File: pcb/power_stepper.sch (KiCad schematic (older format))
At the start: 52 parts, among them J2 1757284, P3 CONN_02X02, U16 UCC12040, U17 ISO7762, U2 powerSTEP01

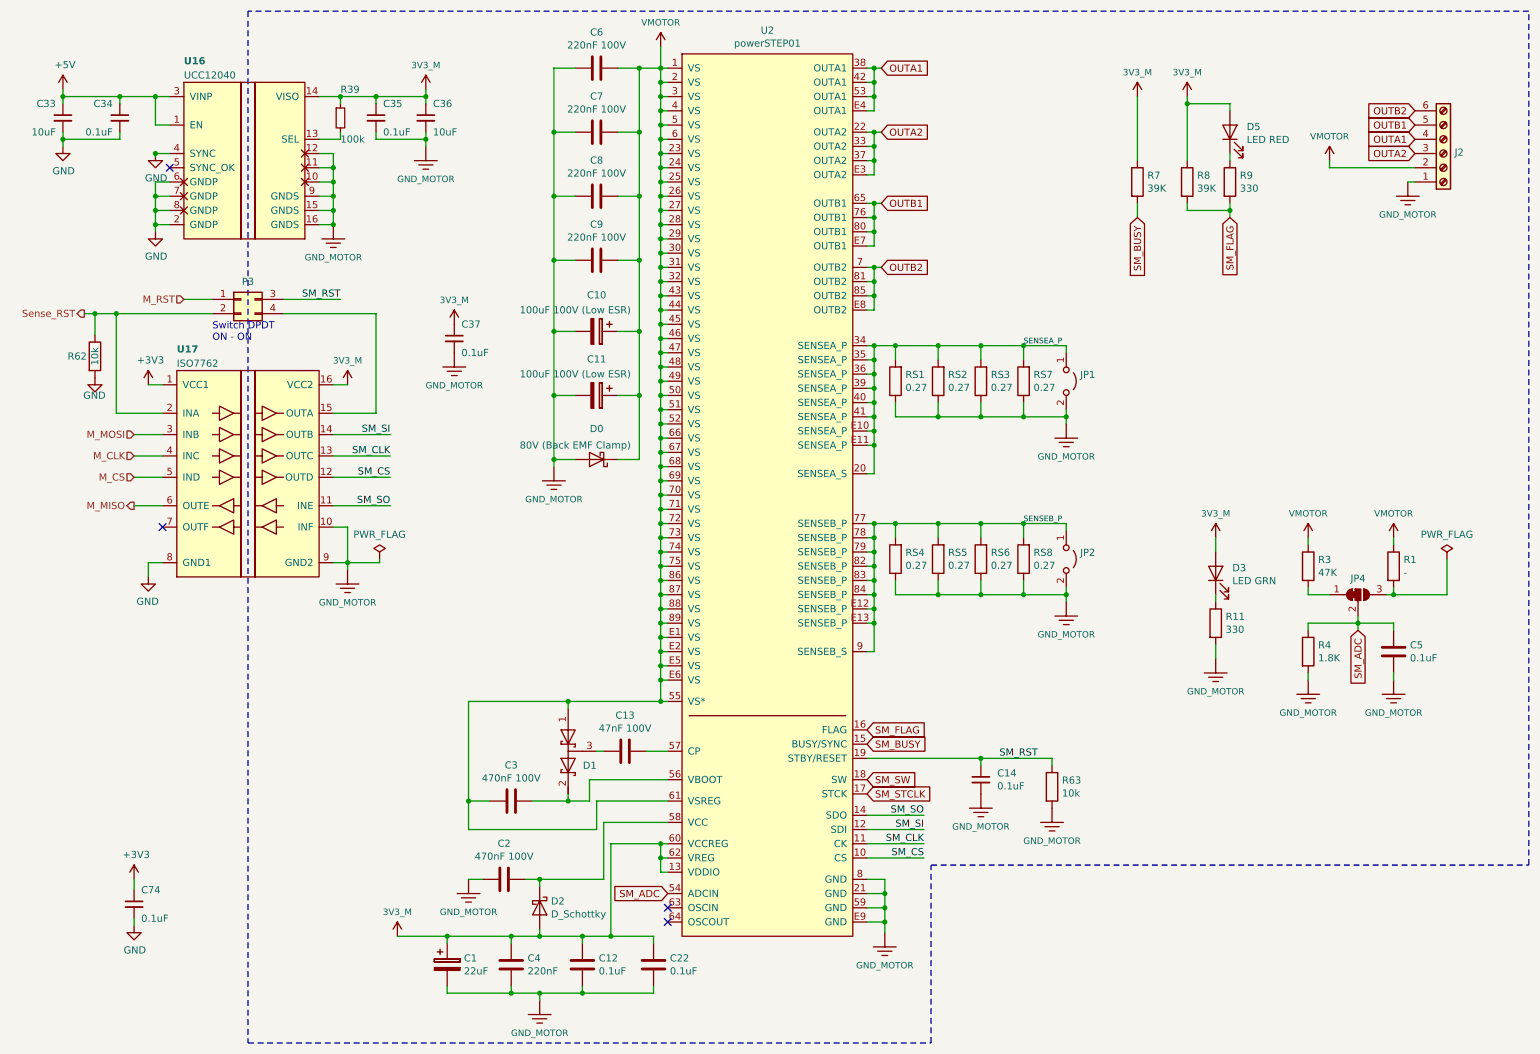
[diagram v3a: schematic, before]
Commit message: Chaged P3 to SW1 and a new circuit to emergency reset on IC powerstep01 Added 3d shape for 2 contancs molex clik-mate connector
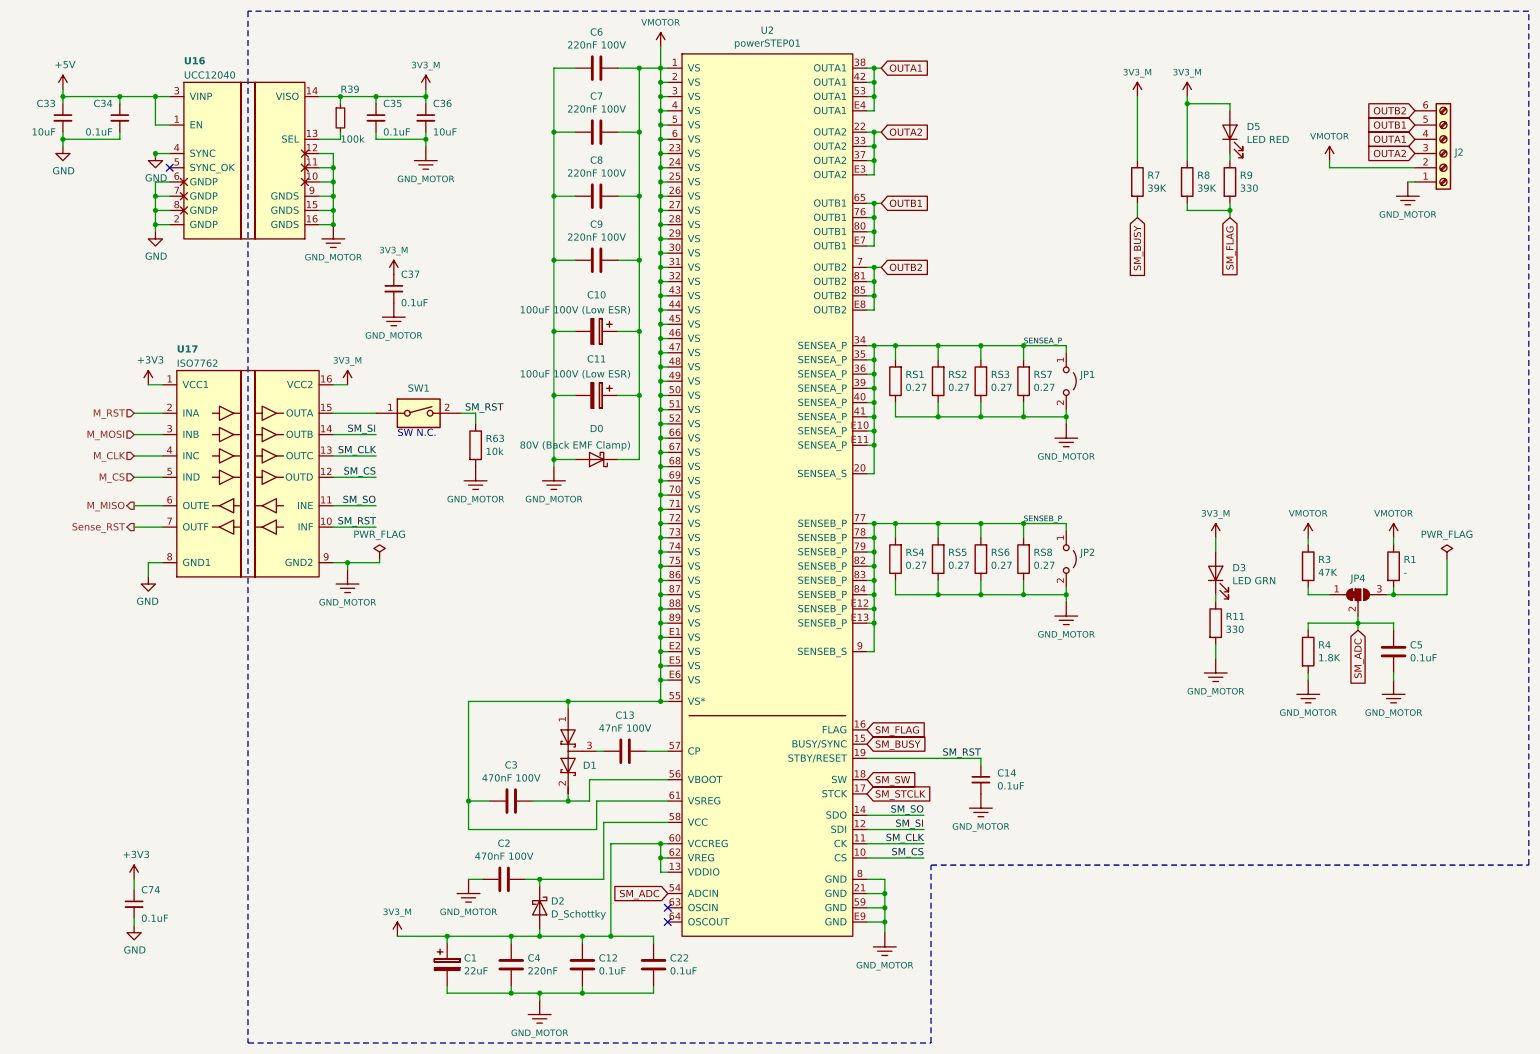
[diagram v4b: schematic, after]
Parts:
- removed P3: CONN_02X02, Connector_Molex:Molex_CLIK-Mate_502443-0470_1x04-1MP_P2.00mm_Vertical, symbol Connector_Generic:Conn_02x02_Top_Bottom
- removed R62: 10k, Resistor_SMD:R_0402_1005Metric, symbol Device:R
- added SW1: SW_DIP_x01, Connector_Molex:Molex_CLIK-Mate_502443-0270_1x02-1MP_P2.00mm_Vertical, symbol Switch:SW_DIP_x01
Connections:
- net GND_MOTOR: no longer U17.10 (INF)
- net M_RST: now also U17.2 (INA)
- net SM_RST: now also U17.10 (INF), SW1.2
- net Sense_RST: now also U17.7 (OUTF); no longer U17.2 (INA)
- net at U17.15 (OUTA): now also SW1.1
- no-connect marks 4 -> 3
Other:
- note added: "SW N.C."
- note removed: "Switch DPDT\nON - ON"
- moved on the sheet: C37, R63
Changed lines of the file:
@@
 Wire Wire Line
 	7250 5800 7250 5750
-Connection ~ 7250 5750
 Wire Wire Line
 	7850 3350 7850 3300
@@
 	2800 4375 2800 4425
 Wire Wire Line
-	2350 2525 2750 2525
-Text Label 2750 2525 2    50   ~ 0
+	3600 3325 3700 3325
+Text Label 3625 3325 0    50   ~ 0
 SM_RST
-Text Label 3100 3625 2    50   ~ 0
+Text Label 3000 3625 2    50   ~ 0
 SM_CLK
 Wire Wire Line
-	2700 3775 3100 3775
-Text Label 3100 3775 2    50   ~ 0
+	2700 3775 3000 3775
+Text Label 3000 3775 2    50   ~ 0
 SM_CS
 Wire Wire Line
-	2700 3975 3100 3975
-Text Label 3100 3975 2    50   ~ 0
+	2700 3975 3000 3975
+Text Label 3000 3975 2    50   ~ 0
 SM_SO
-Text Label 7650 5750 2    50   ~ 0
+Text Label 7250 5750 2    50   ~ 0
 SM_RST
 Wire Wire Line
@@
 L Device:C_Small C37
 U 1 1 5ED0B425
-P 3550 2800
-F 0 "C37" H 3600 2900 50  0000 L CNN
-F 1 "0.1uF" H 3600 2700 50  0000 L CNN
-F 2 "Capacitor_SMD:C_0402_1005Metric" H 3588 2650 50  0001 C CNN
-F 3 "~" H 3550 2800 50  0001 C CNN
-	1    3550 2800
+P 3125 2450
+F 0 "C37" H 3175 2550 50  0000 L CNN
+F 1 "0.1uF" H 3175 2350 50  0000 L CNN
+F 2 "Capacitor_SMD:C_0402_1005Metric" H 3163 2300 50  0001 C CNN
+F 3 "~" H 3125 2450 50  0001 C CNN
+	1    3125 2450
 	1    0    0    -1
 $EndComp
@@
 L ventilator-PowerSymbols:3V3_M #SUPPLY0111
 U 1 1 5ED0B439
-P 3550 2700
-F 0 "#SUPPLY0111" H 3600 2700 45  0001 L BNN
-F 1 "3V3_M" H 3550 2870 45  0000 C CNN
-F 2 "" H 3550 2700 50  0001 C CNN
-F 3 "" H 3550 2700 60  0001 C CNN
-	1    3550 2700
+P 3125 2350
+F 0 "#SUPPLY0111" H 3175 2350 45  0001 L BNN
+F 1 "3V3_M" H 3125 2520 45  0000 C CNN
+F 2 "" H 3125 2350 50  0001 C CNN
+F 3 "" H 3125 2350 60  0001 C CNN
+	1    3125 2350
 	1    0    0    -1
 $EndComp
 Wire Wire Line
 	2700 3125 2800 3125
-NoConn ~ 1500 4125
-Wire Wire Line
-	2700 4125 2800 4125
-Wire Wire Line
-	2800 4125 2800 4375
+Wire Wire Line
+	2700 4125 3000 4125
 Connection ~ 2800 4375
 Text HLabel 1300 3775 0    50   Input ~ 0
 M_CS
-Text HLabel 1650 2525 0    50   Input ~ 0
+Text HLabel 1300 3325 0    50   Input ~ 0
 M_RST
 Text HLabel 1300 3625 0    50   Input ~ 0
@@
 Wire Wire Line
 	1300 3775 1500 3775
-Wire Wire Line
-	1650 2525 1850 2525
 Wire Wire Line
 	1300 3625 1500 3625
@@
 L ventilator-PowerSymbols:GND_MOTOR #GND0114
 U 1 1 5EB73041
-P 3550 2900
-F 0 "#GND0114" H 3600 2850 45  0001 L BNN
-F 1 "GND_MOTOR" H 3550 2670 45  0000 C CNN
-F 2 "" H 3550 2900 50  0001 C CNN
-F 3 "" H 3550 2800 60  0001 C CNN
-	1    3550 2900
+P 3125 2550
+F 0 "#GND0114" H 3175 2500 45  0001 L BNN
+F 1 "GND_MOTOR" H 3125 2320 45  0000 C CNN
+F 2 "" H 3125 2550 50  0001 C CNN
+F 3 "" H 3125 2450 60  0001 C CNN
+	1    3125 2550
 	1    0    0    -1
 $EndComp
@@
 $EndComp
 Wire Wire Line
-	2700 3625 3100 3625
-Wire Wire Line
-	2700 3475 3100 3475
-Text Label 3100 3475 2    50   ~ 0
+	2700 3625 3000 3625
+Wire Wire Line
+	2700 3475 3000 3475
+Text Label 3000 3475 2    50   ~ 0
 SM_SI
 Text Label 7550 4100 0    39   ~ 0
@@
 	2700 1600 2700 1700
 $Comp
-L Connector_Generic:Conn_02x02_Top_Bottom P3
-U 1 1 5EDFFD86
-P 2050 2525
-F 0 "P3" H 2100 2650 50  0000 C CNN
-F 1 "CONN_02X02" H 2050 2699 50  0001 C CNN
-F 2 "Connector_Molex:Molex_CLIK-Mate_502443-0470_1x04-1MP_P2.00mm_Vertical" H 2050 2705 60  0001 C CNN
-F 3 "" H 2050 1325 60  0000 C CNN
-F 4 "WM2278CT-ND" H 2050 2525 50  0001 C CNN "DigiKey"
-F 5 "WM2274-ND" H 2050 2525 50  0001 C CNN "DigiKey_2"
-F 6 "WM3978CT-ND" H 2050 2525 50  0001 C CNN "DigiKey_3"
-	1    2050 2525
-	1    0    0    -1
-$EndComp
-$Comp
 L Device:R R63
 U 1 1 5EE5E424
-P 7750 5950
-F 0 "R63" H 7820 5996 50  0000 L CNN
-F 1 "10k" H 7820 5905 50  0000 L CNN
-F 2 "Resistor_SMD:R_0402_1005Metric" V 7680 5950 50  0001 C CNN
-F 3 "~" H 7750 5950 50  0001 C CNN
-	1    7750 5950
-	1    0    0    -1
-$EndComp
-Wire Wire Line
-	7750 5800 7750 5750
-Wire Wire Line
-	7250 5750 7750 5750
-Wire Wire Line
-	2350 2625 3000 2625
-Wire Wire Line
-	3000 2625 3000 3325
+P 3700 3550
+F 0 "R63" H 3770 3596 50  0000 L CNN
+F 1 "10k" H 3770 3505 50  0000 L CNN
+F 2 "Resistor_SMD:R_0402_1005Metric" V 3630 3550 50  0001 C CNN
+F 3 "~" H 3700 3550 50  0001 C CNN
+	1    3700 3550
+	1    0    0    -1
+$EndComp
 Wire Wire Line
 	3000 3325 2700 3325
 Wire Wire Line
-	1850 2625 1175 2625
-Wire Wire Line
-	1175 2625 1175 3325
-Wire Wire Line
-	1175 3325 1500 3325
-$Comp
-L Device:R R62
-U 1 1 5F0C1C4E
-P 1025 2925
-F 0 "R62" H 900 2925 50  0000 C CNN
-F 1 "10k" V 1025 2925 50  0000 C CNN
-F 2 "Resistor_SMD:R_0402_1005Metric" V 955 2925 50  0001 C CNN
-F 3 "~" H 1025 2925 50  0001 C CNN
-	1    1025 2925
-	1    0    0    -1
-$EndComp
-$Comp
-L power:GND #PWR051
-U 1 1 5F0C2988
-P 1025 3075
-F 0 "#PWR051" H 1025 2825 50  0001 C CNN
-F 1 "GND" H 1100 2950 50  0000 R CNN
-F 2 "" H 1025 3075 50  0001 C CNN
-F 3 "" H 1025 3075 50  0001 C CNN
-	1    1025 3075
-	1    0    0    -1
-$EndComp
-Wire Wire Line
-	1025 2775 1025 2625
-Wire Wire Line
-	1025 2625 1175 2625
-Connection ~ 1175 2625
-Text HLabel 950  2625 0    50   Output ~ 0
+	1300 3325 1500 3325
+Text HLabel 1300 4125 0    50   Output ~ 0
 Sense_RST
-Wire Wire Line
-	950  2625 1025 2625
-Connection ~ 1025 2625
-Text Notes 1850 2825 0    50   ~ 0
-Switch DPDT\nON - ON
-$Comp
-L ventilator-PowerSymbols:GND_MOTOR #GND?
+$Comp
+L ventilator-PowerSymbols:GND_MOTOR #GND01
 U 1 1 5F1D641A
-P 7750 6100
-F 0 "#GND?" H 7800 6050 45  0001 L BNN
-F 1 "GND_MOTOR" H 7750 5870 45  0000 C CNN
-F 2 "" H 7750 6100 50  0001 C CNN
-F 3 "" H 7750 6000 60  0001 C CNN
-	1    7750 6100
-	1    0    0    -1
-$EndComp
+P 3700 3700
+F 0 "#GND01" H 3750 3650 45  0001 L BNN
+F 1 "GND_MOTOR" H 3700 3470 45  0000 C CNN
+F 2 "" H 3700 3700 50  0001 C CNN
+F 3 "" H 3700 3600 60  0001 C CNN
+	1    3700 3700
+	1    0    0    -1
+$EndComp
+$Comp
+L Switch:SW_DIP_x01 SW1
+U 1 1 5EE843B4
+P 3300 3325
+F 0 "SW1" H 3300 3500 50  0000 C CNN
+F 1 "SW_DIP_x01" H 3300 3501 50  0001 C CNN
+F 2 "Connector_Molex:Molex_CLIK-Mate_502443-0270_1x02-1MP_P2.00mm_Vertical" H 3300 3325 50  0001 C CNN
+F 3 "" H 3300 3325 50  0001 C CNN
+F 4 "WM15808CT-ND" H 3300 3325 50  0001 C CNN "DigiKey"
+F 5 "900-5024390200-ND" H 3300 3325 50  0001 C CNN "DigiKey2"
+F 6 "WM3978CT-ND" H 3300 3325 50  0001 C CNN "DigiKey3"
+	1    3300 3325
+	1    0    0    -1
+$EndComp
+Wire Wire Line
+	1500 4125 1300 4125
+Text Notes 3150 3500 0    50   ~ 0
+SW N.C.
+Wire Wire Line
+	3700 3400 3700 3325
+Text Label 3000 4125 2    50   ~ 0
+SM_RST
 $EndSCHEMATC

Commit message: Added components dikey part numbers in modified sheets
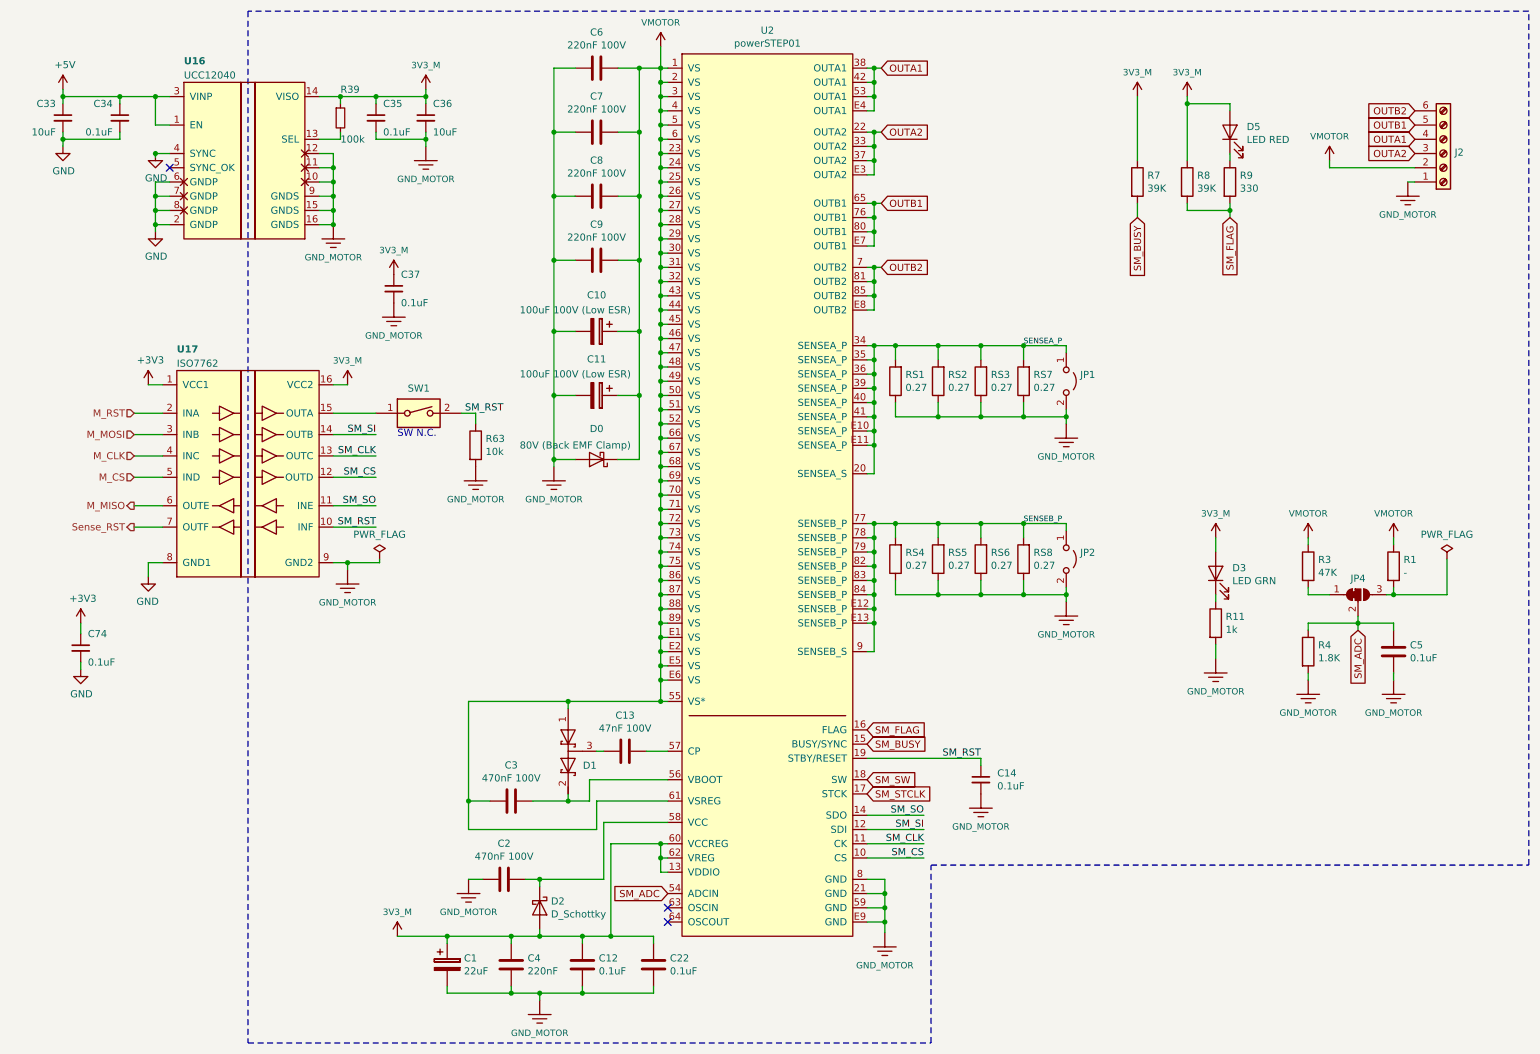
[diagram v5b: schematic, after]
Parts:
- C1: DigiKey (none) -> 1276-1100-1-ND
- C10, C11: DigiKey (none) -> P10776-ND
- C12, C14, C22, C34, C35, C37, C74: DigiKey (none) -> 1276-1442-1-ND
- C13: DigiKey (none) -> 1276-2960-1-ND
- C2, C3: DigiKey (none) -> 478-9924-1-ND
- C33, C36: DigiKey (none) -> 478-10766-1-ND
- C4: DigiKey (none) -> 1276-1539-1-ND
- C5: DigiKey (none) -> 1276-1258-1-ND
- C6, C7, C8, C9: DigiKey (none) -> 1276-2949-1-ND
- D0: DigiKey (none) -> B280-FDICT-ND
- D1: DigiKey (none) -> 1514-CMPSH1-4TRPBFREECT-ND
- D2: DigiKey (none) -> 1727-7336-1-ND
- D3: DigiKey (none) -> SML-D12M1WT86CT-ND
- D5: DigiKey (none) -> SML-D12U1WT86CT-ND
- J2: DigiKey 1757284 -> 277-1110-ND
- R11: value 330 -> 1k; DigiKey (none) -> P1.0KJCT-ND
- R3: DigiKey (none) -> P47KGCT-ND
- R39: DIgiKey (none) -> P100KJCT-ND
- R4: DigiKey (none) -> P1.8KGCT-ND
- R63: DigiKey (none) -> 311-10KJRCT-ND
- R7, R8: DigiKey (none) -> P39KJCT-ND
- R9: DigiKey (none) -> P330LCT-ND
- RS1, RS2, RS3, RS4, RS5, RS6, RS7, RS8: DigiKey (none) -> PT.27UDKR-ND
- U16: DigiKey (none) -> 296-UCC12040DVERCT-ND
- U17: DigiKey (none) -> 296-49452-1-ND
- U2: DigiKey (none) -> 497-15441-ND
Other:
- moved on the sheet: C74

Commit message: Added digiKey part number for some components
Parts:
- R63: DigiKey 311-10KJRCT-ND -> P10KJDKR-ND
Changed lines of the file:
@@
 F 2 "Resistor_SMD:R_0402_1005Metric" V 3630 3550 50  0001 C CNN
 F 3 "~" H 3700 3550 50  0001 C CNN
-F 4 "311-10KJRCT-ND" H 3700 3550 50  0001 C CNN "DigiKey"
+F 4 "P10KJDKR-ND" H 3700 3550 50  0001 C CNN "DigiKey"
 	1    3700 3550
 	1    0    0    -1

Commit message: Added all references on silkscreen added BOM for sensor modules
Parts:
- R39: DIgiKey P100KJCT-ND -> (none); DigiKey (none) -> P100KJCT-ND
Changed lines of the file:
@@
 F 2 "Resistor_SMD:R_0402_1005Metric" H 2750 1250 50  0001 C CNN
 F 3 "~" H 2750 1250 50  0001 C CNN
-F 4 "P100KJCT-ND" H 2750 1250 50  0001 C CNN "DIgiKey"
+F 4 "P100KJCT-ND" H 2750 1250 50  0001 C CNN "DigiKey"
 	1    2750 1250
 	1    0    0    -1

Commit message: Added kicad design with 4 pressure sensors for daugthers PCB Added DigiKey number for power connector
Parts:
- J2: DigiKey2 (none) -> 277-1015-ND
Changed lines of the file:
@@
 F 3 "~" H 10500 1500 50  0001 C CNN
 F 4 "277-1110-ND" H 10500 1500 50  0001 C CNN "DigiKey"
+F 5 "277-1015-ND" H 10500 1500 50  0001 C CNN "DigiKey2"
 	1    10500 1500
 	1    0    0    1
